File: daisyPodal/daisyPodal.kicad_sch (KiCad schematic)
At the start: 45 parts, among them J1 Guitar in, J2 Left out, J3 fsw pin 1, J4 fsw pin 4, J5 fsw pin 6, J6 fsw pin 3, J7 fsw pin 2, J8 fsw pin 5, SW1 Switch 1, SW2 Switch 2, SW3 RotaryEncoder_Switch, U1 L78L05_TO92, U2 TL072

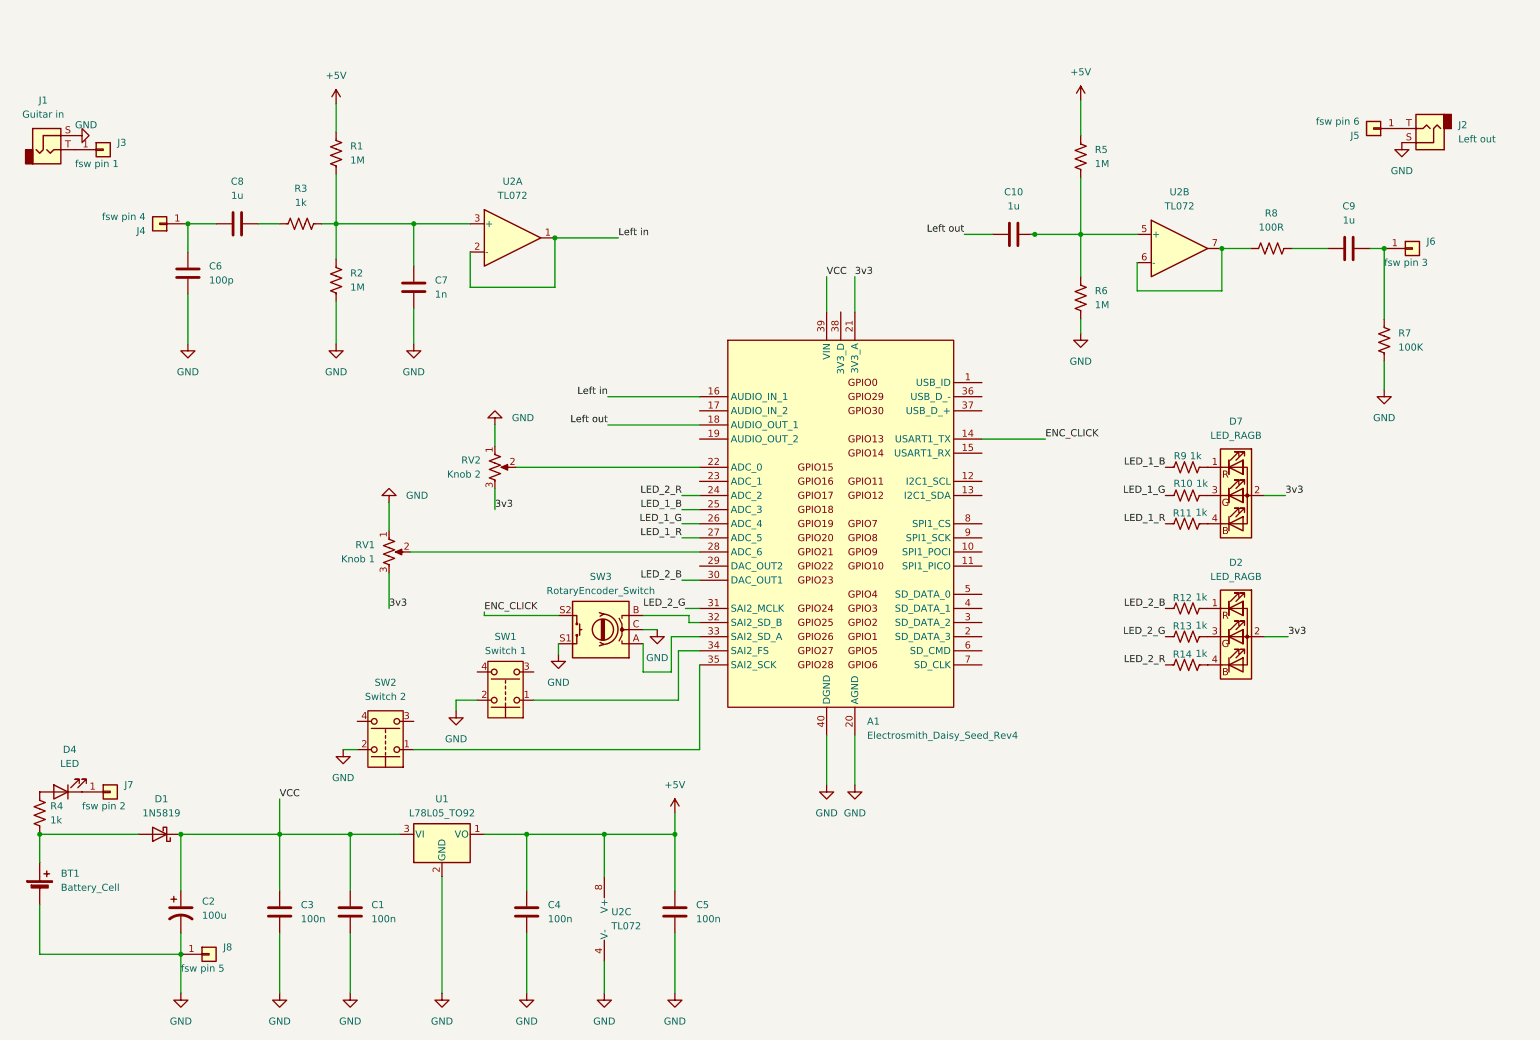
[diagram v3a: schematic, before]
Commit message: Add right out - stereo now
Replaced TL072 with TL074
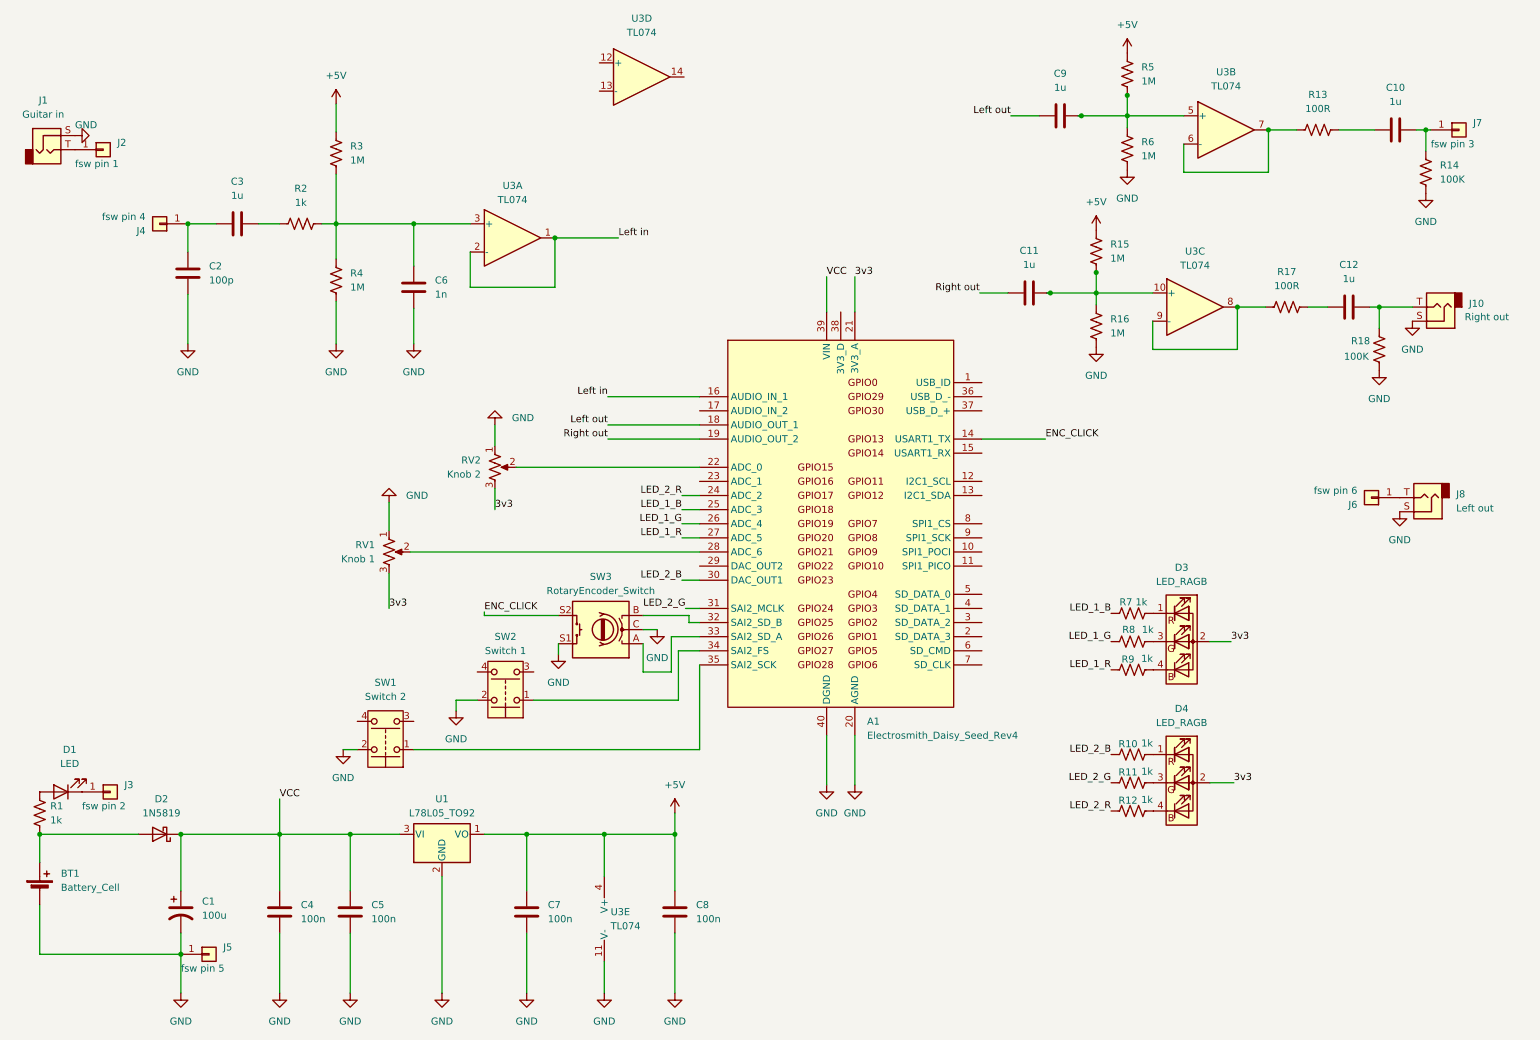
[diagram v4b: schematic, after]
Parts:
- removed U2: TL072, Package_DIP:DIP-8_W7.62mm_Socket, symbol Amplifier_Operational:TL072
- added C11, C12: 1u, Capacitor_THT:C_Rect_L9.0mm_W2.5mm_P7.50mm_MKT, symbol Device:C
- added J10: Right out, Connector_Audio:Jack_6.35mm_Neutrik_NRJ6HM-1_Horizontal, symbol Connector_Audio:AudioJack2
- added R15, R16: 1M, Resistor_THT:R_Axial_DIN0207_L6.3mm_D2.5mm_P10.16mm_Horizontal, symbol Device:R_US
- added R17: 100R, Resistor_THT:R_Axial_DIN0207_L6.3mm_D2.5mm_P10.16mm_Horizontal, symbol Device:R_US
- added R18: 100K, Resistor_THT:R_Axial_DIN0207_L6.3mm_D2.5mm_P10.16mm_Horizontal, symbol Device:R_US
- added U3: TL074, Package_DIP:DIP-14_W7.62mm_Socket, symbol Amplifier_Operational:TL074
- D3: renamed from D7; footprint (none) -> LED_THT:LED_D5.0mm-4_RGB
- D4: renamed from D2; footprint (none) -> LED_THT:LED_D5.0mm-4_RGB
- U1: footprint Package_TO_SOT_THT:TO-92_Inline_Wide -> Package_TO_SOT_THT:TO-92_Inline_Wide_78L05_dc
- renumbered C2 to C1, C9 to C10, C6 to C2, C8 to C3, C3 to C4, C1 to C5, C7 to C6, C4 to C7, C5 to C8, C10 to C9, D4 to D1, D1 to D2, J3 to J2, J7 to J3, J8 to J5, J5 to J6, J6 to J7, J2 to J8, R4 to R1, R12 to R10, R13 to R11, R14 to R12, R8 to R13, R7 to R14, R3 to R2, R1 to R3, R2 to R4, R9 to R7, R10 to R8, R11 to R9, SW2 to SW1, SW1 to SW2
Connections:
- net +5V: now also R15.1, U3.4 (V+)
- net GND: now also J10.S, R16.2, R18.2, U3.11 (V-)
- net Left in: now also U3.1, U3.2 (-)
- net at R13.1: now also U3.6 (-), U3.7
- net at C6.1, R2.2, R3.2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: now also U3.3 (+)
- net at C9.2, R5.2, R6.1: now also U3.5 (+)
- net Right out: now reaches A1.19 (AUDIO_OUT_2)
- net Right out: now also C11.1
- new net: C11.2, R15.2, R16.1, U3.10 (+)
- new net: C12.2, J10.T, R18.1
- new net: R17.1, U3.8, U3.9 (-)
- new net: C12.1, R17.2
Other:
- moved on the sheet: C10, C9, D3, D4, J6, J7, J8, R10, R11, R12, R13, R14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

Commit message: reduce size of box capacitors to fit caps we use
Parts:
- removed unit 4 of U3
- C10: renamed from C9; footprint Capacitor_THT:C_Rect_L9.0mm_W2.5mm_P7.50mm_MKT -> Capacitor_THT:C_Rect_L7.0mm_W2.5mm_P5.00mm
- C11: renamed from C12; footprint Capacitor_THT:C_Rect_L9.0mm_W2.5mm_P7.50mm_MKT -> Capacitor_THT:C_Rect_L7.0mm_W2.5mm_P5.00mm
- C12: renamed from C10; footprint Capacitor_THT:C_Rect_L9.0mm_W2.5mm_P7.50mm_MKT -> Capacitor_THT:C_Rect_L7.0mm_W2.5mm_P5.00mm
- C2, C3, C4, C5, C6, C7, C8: footprint Capacitor_THT:C_Rect_L9.0mm_W2.5mm_P7.50mm_MKT -> Capacitor_THT:C_Rect_L7.0mm_W2.5mm_P5.00mm
- C9: renamed from C11; footprint Capacitor_THT:C_Rect_L9.0mm_W2.5mm_P7.50mm_MKT -> Capacitor_THT:C_Rect_L7.0mm_W2.5mm_P5.00mm
- renumbered J8 to J7, J10 to J8, J7 to J9, R8 to R10, R9 to R11, R10 to R12, R11 to R13, R12 to R14, R17 to R15, R13 to R16, R18 to R17, R14 to R18, R15 to R5, R16 to R6, R5 to R7, R6 to R8, R7 to R9, U3 to U2
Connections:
- net at C6.1, R2.2, U2.3 (+): no longer R3.2, R4.1
- new net: R3.2, R4.1

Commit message: Place components on PCB in sensible blocks
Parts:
- SW1: renamed from SW2; footprint Button_Switch_THT:SW_CW_GPTS203211B_1 podal -> Connector_Wire:SolderWire-0.75sqmm_1x02_P7mm_D1.25mm_OD3.5mm
- SW2: renamed from SW1; footprint Button_Switch_THT:SW_CW_GPTS203211B_1 podal -> Connector_Wire:SolderWire-0.75sqmm_1x02_P7mm_D1.25mm_OD3.5mm
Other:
- moved on the sheet: SW2
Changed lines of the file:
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@@
+    (stroke (width 0) (type default))
+  )
+  (wire (pts (xy 137.16 148.59) (xy 119.253 148.59))
     (stroke (width 0) (type default))
   )
@@
     (stroke (width 0) (type default))
   )
-  (wire (pts (xy 73.025 146.05) (xy 75.565 146.05))
+  (wire (pts (xy 106.553 148.59) (xy 109.093 148.59))
     (stroke (width 0) (type default))
   )
@@
     (stroke (width 0) (type default))
   )
-  (wire (pts (xy 85.725 146.05) (xy 137.16 146.05))
-    (stroke (width 0) (type default))
-  )
   (wire (pts (xy 266.192 34.544) (xy 267.843 34.544))
     (stroke (width 0) (type default))
@@
     (stroke (width 0) (type default))
   )
-  (wire (pts (xy 137.16 130.81) (xy 137.16 146.05))
+  (wire (pts (xy 137.16 130.81) (xy 137.16 148.59))
     (stroke (width 0) (type default))
   )
@@
     )
   )
-  (symbol (lib_id "power:GND") (at 73.025 146.05 0) (unit 1)
-    (in_bom yes) (on_board yes) (dnp no) (fields_autoplaced)
-    (property "Reference" "#PWR07" (at 73.025 152.4 0)
-      (effects (font (size 1.27 1.27)) hide)
-    )
-    (property "Value" "GND" (at 73.025 151.13 0)
-      (effects (font (size 1.27 1.27)))
-    )
-    (property "Footprint" "" (at 73.025 146.05 0)
-      (effects (font (size 1.27 1.27)) hide)
-    )
-    (property "Datasheet" "" (at 73.025 146.05 0)
-      (effects (font (size 1.27 1.27)) hide)
-    )
-    (pin "1")
-    (instances
-      (project "daisyPodal"
-        (path "/12e895f7-e5ae-4934-aed6-e6e04c63dd03"
-          (reference "#PWR07") (unit 1)
+  (symbol (lib_id "power:GND") (at 106.553 148.59 0) (unit 1)
+    (in_bom yes) (on_board yes) (dnp no) (fields_autoplaced)
+    (property "Reference" "#PWR014" (at 106.553 154.94 0)
+      (effects (font (size 1.27 1.27)) hide)
+    )
+    (property "Value" "GND" (at 106.553 153.67 0)
+      (effects (font (size 1.27 1.27)))
+    )
+    (property "Footprint" "" (at 106.553 148.59 0)
+      (effects (font (size 1.27 1.27)) hide)
+    )
+    (property "Datasheet" "" (at 106.553 148.59 0)
+      (effects (font (size 1.27 1.27)) hide)
+    )
+    (pin "1")
+    (instances
+      (project "daisyPodal"
+        (path "/12e895f7-e5ae-4934-aed6-e6e04c63dd03"
+          (reference "#PWR014") (unit 1)
         )
       )
@@
   (symbol (lib_id "power:GND") (at 85.725 73.025 0) (unit 1)
     (in_bom yes) (on_board yes) (dnp no) (fields_autoplaced)
-    (property "Reference" "#PWR010" (at 85.725 79.375 0)
+    (property "Reference" "#PWR09" (at 85.725 79.375 0)
       (effects (font (size 1.27 1.27)) hide)
     )
@@
       (project "daisyPodal"
         (path "/12e895f7-e5ae-4934-aed6-e6e04c63dd03"
-          (reference "#PWR010") (unit 1)
+          (reference "#PWR09") (unit 1)
         )
       )
@@
   (symbol (lib_id "power:GND") (at 93.345 139.065 0) (unit 1)
     (in_bom yes) (on_board yes) (dnp no) (fields_autoplaced)
-    (property "Reference" "#PWR012" (at 93.345 145.415 0)
+    (property "Reference" "#PWR011" (at 93.345 145.415 0)
       (effects (font (size 1.27 1.27)) hide)
     )
@@
       (project "daisyPodal"
         (path "/12e895f7-e5ae-4934-aed6-e6e04c63dd03"
-          (reference "#PWR012") (unit 1)
+          (reference "#PWR011") (unit 1)
         )
       )
@@
   (symbol (lib_id "power:GND") (at 74.295 189.865 0) (unit 1)
     (in_bom yes) (on_board yes) (dnp no) (fields_autoplaced)
-    (property "Reference" "#PWR08" (at 74.295 196.215 0)
+    (property "Reference" "#PWR07" (at 74.295 196.215 0)
       (effects (font (size 1.27 1.27)) hide)
     )
@@
       (project "daisyPodal"
         (path "/12e895f7-e5ae-4934-aed6-e6e04c63dd03"
-          (reference "#PWR08") (unit 1)
+          (reference "#PWR07") (unit 1)
         )
       )
@@
     )
   )
-  (symbol (lib_id "Switch:SW_Push_Dual") (at 80.645 143.51 180) (unit 1)
-    (in_bom yes) (on_board yes) (dnp no) (fields_autoplaced)
-    (property "Reference" "SW1" (at 80.645 133.985 0)
-      (effects (font (size 1.27 1.27)))
-    )
-    (property "Value" "Switch 2" (at 80.645 136.525 0)
-      (effects (font (size 1.27 1.27)))
-    )
-    (property "Footprint" "Button_Switch_THT:SW_CW_GPTS203211B_1 podal" (at 80.645 151.13 0)
-      (effects (font (size 1.27 1.27)) hide)
-    )
-    (property "Datasheet" "~" (at 80.645 143.51 0)
+  (symbol (lib_id "Switch:SW_Push_Dual") (at 114.173 146.05 180) (unit 1)
+    (in_bom yes) (on_board yes) (dnp no)
+    (property "Reference" "SW2" (at 106.934 145.669 0)
+      (effects (font (size 1.27 1.27)))
+    )
+    (property "Value" "Switch 2" (at 114.3 139.954 0)
+      (effects (font (size 1.27 1.27)))
+    )
+    (property "Footprint" "Connector_Wire:SolderWire-0.75sqmm_1x02_P7mm_D1.25mm_OD3.5mm" (at 114.173 153.67 0)
+      (effects (font (size 1.27 1.27)) hide)
+    )
+    (property "Datasheet" "~" (at 114.173 146.05 0)
       (effects (font (size 1.27 1.27)) hide)
     )
@@
       (project "daisyPodal"
         (path "/12e895f7-e5ae-4934-aed6-e6e04c63dd03"
-          (reference "SW1") (unit 1)
+          (reference "SW2") (unit 1)
         )
       )
@@
   (symbol (lib_id "power:GND") (at 106.045 189.865 0) (unit 1)
     (in_bom yes) (on_board yes) (dnp no) (fields_autoplaced)
-    (property "Reference" "#PWR014" (at 106.045 196.215 0)
+    (property "Reference" "#PWR013" (at 106.045 196.215 0)
       (effects (font (size 1.27 1.27)) hide)
     )
@@
       (project "daisyPodal"
         (path "/12e895f7-e5ae-4934-aed6-e6e04c63dd03"
-          (reference "#PWR014") (unit 1)
+          (reference "#PWR013") (unit 1)
         )
       )
@@
   (symbol (lib_id "power:GND") (at 100.33 87.63 180) (unit 1)
     (in_bom yes) (on_board yes) (dnp no) (fields_autoplaced)
-    (property "Reference" "#PWR013" (at 100.33 81.28 0)
+    (property "Reference" "#PWR012" (at 100.33 81.28 0)
       (effects (font (size 1.27 1.27)) hide)
     )
@@
       (project "daisyPodal"
         (path "/12e895f7-e5ae-4934-aed6-e6e04c63dd03"
-          (reference "#PWR013") (unit 1)
+          (reference "#PWR012") (unit 1)
         )
       )
@@
   (symbol (lib_id "power:GND") (at 81.28 101.6 180) (unit 1)
     (in_bom yes) (on_board yes) (dnp no) (fields_autoplaced)
-    (property "Reference" "#PWR09" (at 81.28 95.25 0)
+    (property "Reference" "#PWR08" (at 81.28 95.25 0)
       (effects (font (size 1.27 1.27)) hide)
     )
@@
       (project "daisyPodal"
         (path "/12e895f7-e5ae-4934-aed6-e6e04c63dd03"
-          (reference "#PWR09") (unit 1)
+          (reference "#PWR08") (unit 1)
         )
       )
@@
   (symbol (lib_id "Switch:SW_Push_Dual") (at 102.235 134.62 180) (unit 1)
     (in_bom yes) (on_board yes) (dnp no) (fields_autoplaced)
-    (property "Reference" "SW2" (at 102.235 125.73 0)
+    (property "Reference" "SW1" (at 102.235 125.73 0)
       (effects (font (size 1.27 1.27)))
     )
@@
       (effects (font (size 1.27 1.27)))
     )
-    (property "Footprint" "Button_Switch_THT:SW_CW_GPTS203211B_1 podal" (at 102.235 142.24 0)
+    (property "Footprint" "Connector_Wire:SolderWire-0.75sqmm_1x02_P7mm_D1.25mm_OD3.5mm" (at 102.235 142.24 0)
       (effects (font (size 1.27 1.27)) hide)
     )
@@
       (project "daisyPodal"
         (path "/12e895f7-e5ae-4934-aed6-e6e04c63dd03"
-          (reference "SW2") (unit 1)
+          (reference "SW1") (unit 1)
         )
       )
@@
   (symbol (lib_id "power:GND") (at 90.805 189.865 0) (unit 1)
     (in_bom yes) (on_board yes) (dnp no) (fields_autoplaced)
-    (property "Reference" "#PWR011" (at 90.805 196.215 0)
+    (property "Reference" "#PWR010" (at 90.805 196.215 0)
       (effects (font (size 1.27 1.27)) hide)
     )
@@
       (project "daisyPodal"
         (path "/12e895f7-e5ae-4934-aed6-e6e04c63dd03"
-          (reference "#PWR011") (unit 1)
-        )
-      )
+          (reference "#PWR010") (unit 1)
+        )
+      )

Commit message: Fix input buffer circuit and re-jig PCB
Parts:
- removed C2: 100p, Capacitor_THT:C_Rect_L7.0mm_W2.5mm_P5.00mm, symbol Device:C
- removed C6: 1n, Capacitor_THT:C_Rect_L7.0mm_W2.5mm_P5.00mm, symbol Device:C
- R2: value 1k -> 1M
- renumbered C12 to C10, C3 to C2, C4 to C3, C5 to C4, C7 to C5, C8 to C6, C9 to C7, C10 to C8, C11 to C9, U2 to U1, U1 to U2
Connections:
- net GND: now also R2.2
- net Left in: no longer U1.2 (-)
- net at R3.2, R4.1: now also C2.2, U1.3 (+)
- net at C2.1, J4.1 (Pin_1): now also R2.1
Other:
- moved on the sheet: C2, J4, R3, R4, U1A
